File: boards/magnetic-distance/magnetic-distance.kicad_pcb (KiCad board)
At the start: 2 copper layers, 23 x 19.5 mm, 7 parts, among them J1 CONN_02X03, M3 MountingHole_3.2mm_M3, U1 DS9638, U2 AS5304

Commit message: boards/magnetic-distance: reworked sensor placement, updated schematic export
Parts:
- moved AO 5.12 mm to (185.4, 108.0)
- moved U2 1.81 mm to (190.5, 106.5), turned to 0 degrees
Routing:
- net (no net): track 0.00 -> 17.0 mm, vias 23 -> 15
- net /VCC: track 31.3 -> 38.8 mm
- net /GND: track 8.11 -> 10.6 mm
- net /B_c: track 14.9 -> 13.3 mm

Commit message: [docs] export all board layouts
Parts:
- moved J1 127.0 mm to (64.1, 48.3)
- moved AO 127.0 mm to (69.8, 55.2)
- moved C1 127.0 mm to (65.4, 54.9)
- moved U2 127.0 mm to (74.9, 53.8)
- moved M3 127.0 mm to (70.8, 42.1)
- moved M3 127.0 mm to (64.8, 42.1)
- moved U1 127.0 mm to (61.0, 55.9)
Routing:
- net (no net): track 17.0 -> 18.5 mm
- net /GND: track 10.6 -> 9.10 mm

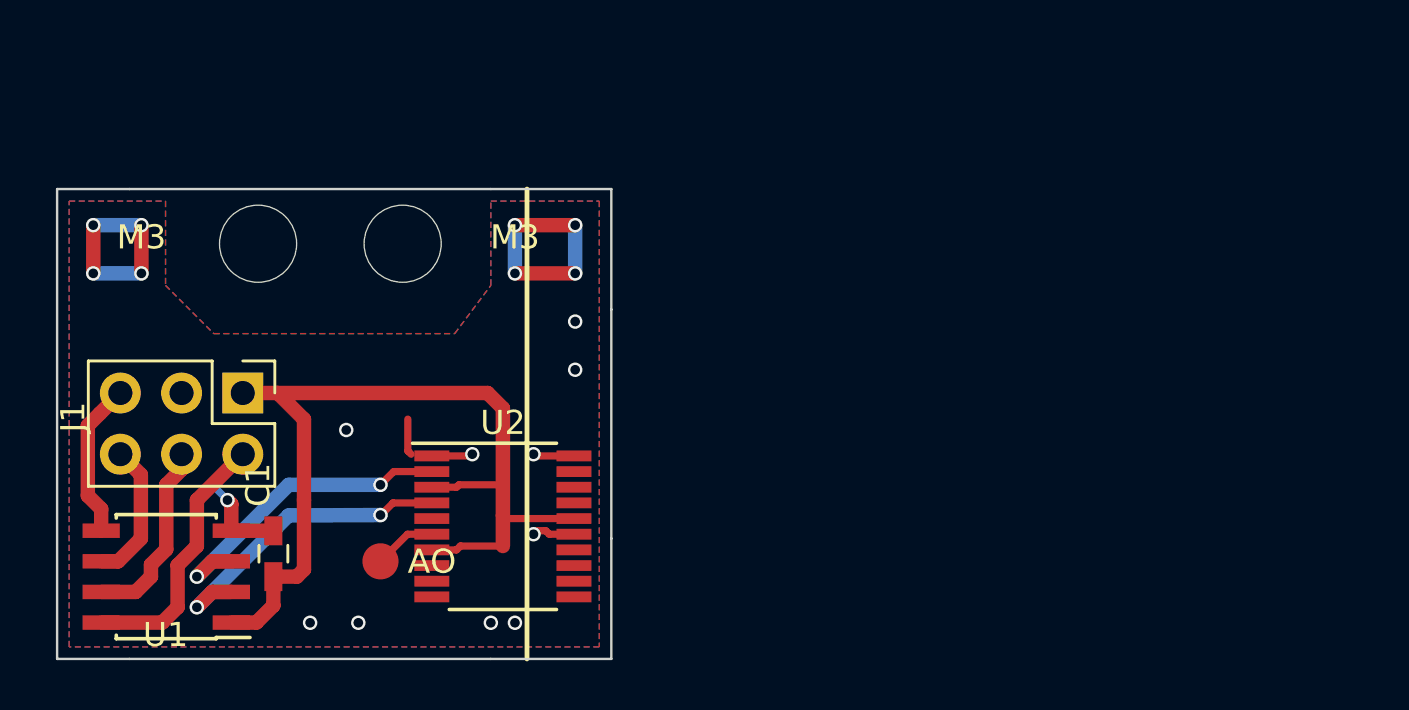
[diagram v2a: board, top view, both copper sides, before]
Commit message: [board][magnetic-distance] remove diff line driver, new board outline
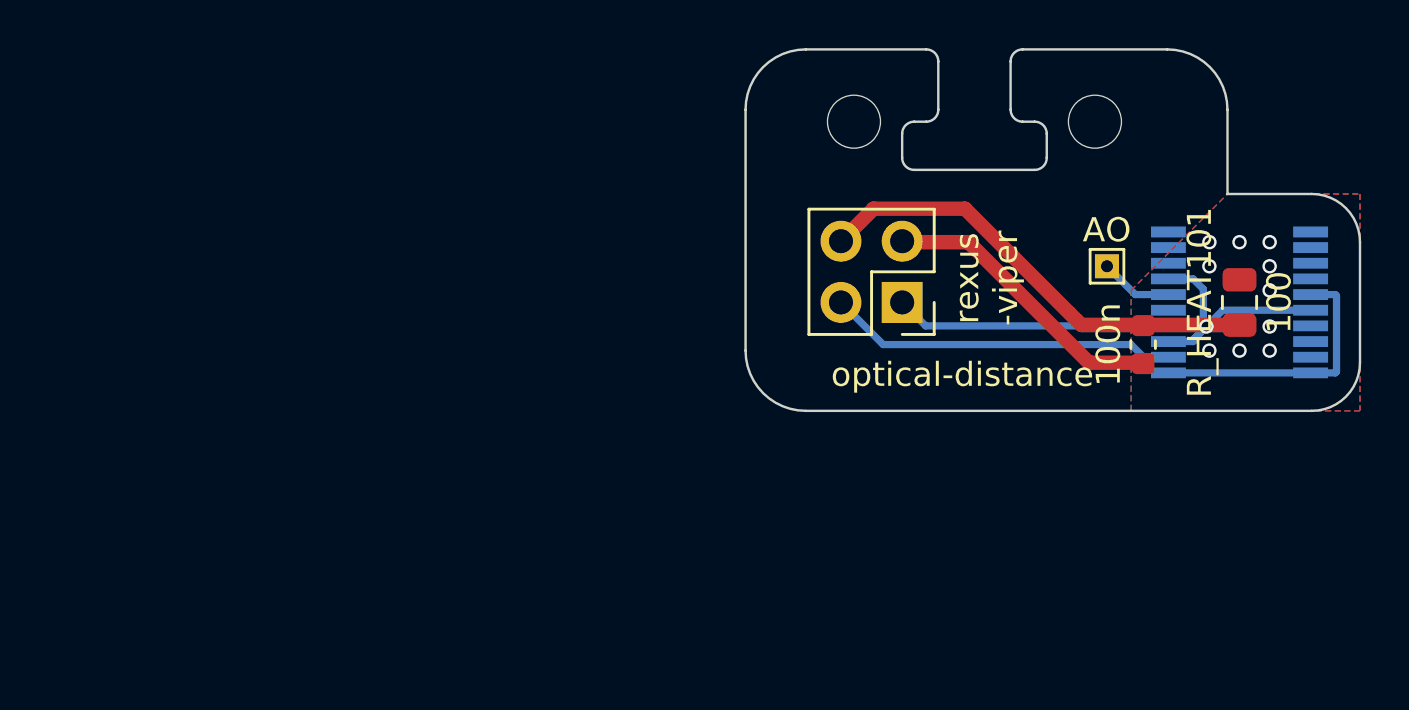
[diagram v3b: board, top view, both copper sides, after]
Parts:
- removed AO: AO, Measurement_Points:Measurement_Point_Round-SMD-Pad_Small
- removed C1: 100nF, Capacitors_SMD:C_0603_HandSoldering
- removed J1: CONN_02X03, Pin_Headers:Pin_Header_Straight_2x03_Pitch2.54mm
- removed M3 (x2): MountingHole_3.2mm_M3, Mounting_Holes:MountingHole_3.2mm_M3
- removed U1: DS9638, Housings_SOIC:SOIC-8_3.9x4.9mm_Pitch1.27mm
- removed U2: AS5304, Housings_SSOP:TSSOP-20_4.4x6.5mm_Pitch0.65mm
- added C101: 100n, Capacitor_SMD:C_0603_1608Metric, F.Cu at (101.5, 46.2)
- added H101: M2, MountingHole:MountingHole_2.2mm_M2, F.Cu at (89.5, 37.0)
- added H102: M2, MountingHole:MountingHole_2.2mm_M2, F.Cu at (99.5, 37.0)
- added J101: Cable, Connector_PinHeader_2.54mm:PinHeader_2x02_P2.54mm_Vertical, F.Cu at (91.5, 44.5)
- added R_HEAT101: 100, Resistor_SMD:R_0805_2012Metric, F.Cu at (105.5, 44.5)
- added TP101: AO, TestPoint:TestPoint_THTPad_1.0x1.0mm_Drill0.5mm, F.Cu at (100.0, 43.0)
- added U101: AS5304, Package_SO:TSSOP-20_4.4x6.5mm_P0.65mm, B.Cu at (105.5, 44.5)
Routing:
- net /VCC: track 38.8 -> 0.00 mm
- net +5V: track 0.00 -> 29.4 mm, vias 0 -> 1
- net GND: track 0.00 -> 23.3 mm, vias 0 -> 10
- net (no net): track 18.5 -> 0.00 mm, vias 15 -> 0
- net /B_c: track 13.3 -> 0.00 mm, vias 2 -> 0
- net /A_c: track 13.2 -> 0.00 mm, vias 2 -> 0
- net /GND: track 9.10 -> 0.00 mm, vias 4 -> 0
- net /A*: track 7.93 -> 0.00 mm
- net /B*: track 6.50 -> 0.00 mm
- net /B: track 5.89 -> 11.5 mm
- net /A: track 10.9 -> 14.5 mm
- added copper zone on B.Cu, net GND
- added copper zone on F.Cu, net GND
- removed copper zone on B.Cu, net /GND
- removed copper zone on F.Cu, net /GND
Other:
- board size 23 x 19.5 mm -> 25.5 x 15 mm
- net class Thin removed
- board text added: "5V"
- board text added: "optical-distance"
- board text added: "rev20"
- board text added: "rexus -viper"
- board text removed: "A*"
- board text removed: "B*"
- board text removed: "VCC"
- board text removed: "rexus-viper magnetic-dis- tance board ©rleh, rchojetzki"

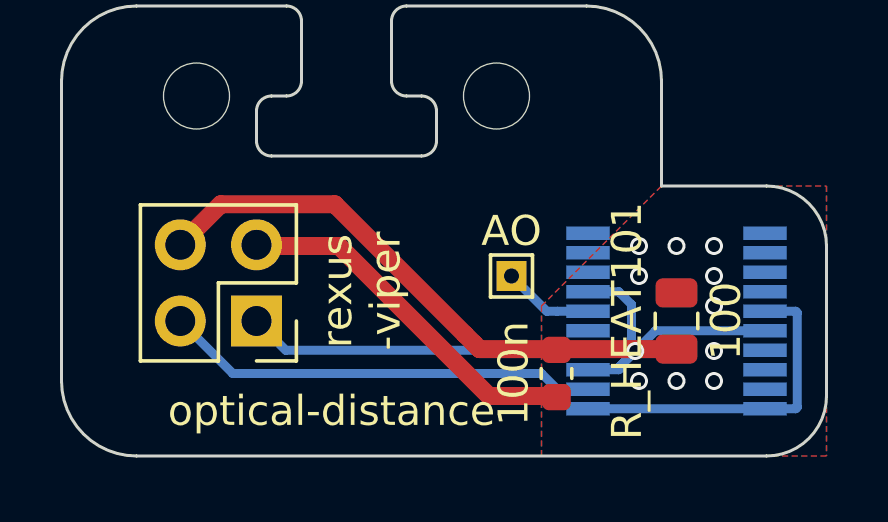
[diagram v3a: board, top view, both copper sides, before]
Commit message: [board][magnetic-distance] sensor placement
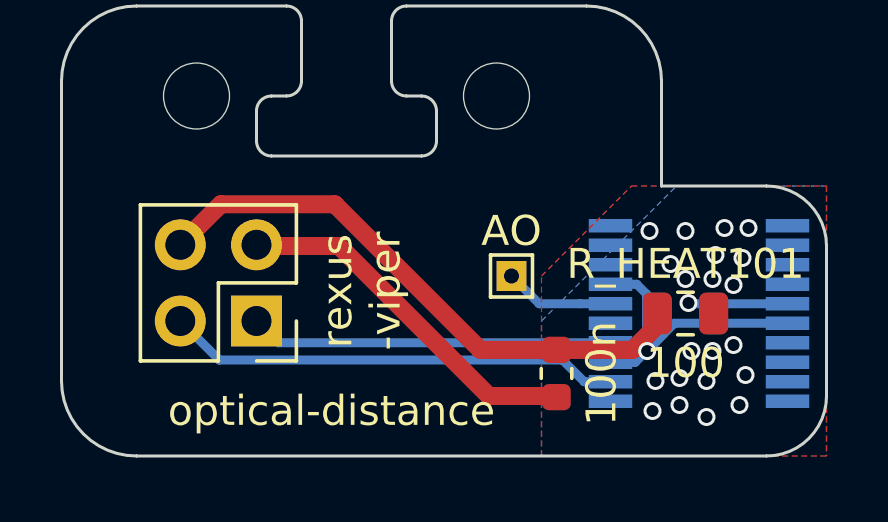
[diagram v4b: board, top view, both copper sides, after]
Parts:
- moved U101 0.79 mm to (106.2, 44.2)
- moved R_HEAT101 0.39 mm to (105.8, 44.2), turned to 0 degrees
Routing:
- net GND: track 23.3 -> 15.6 mm, vias 10 -> 22
- net +5V: track 29.4 -> 31.9 mm
- net /A: track 14.5 -> 15.2 mm
- net /AO: track 3.04 -> 3.68 mm
- net /B: track 11.5 -> 12.1 mm

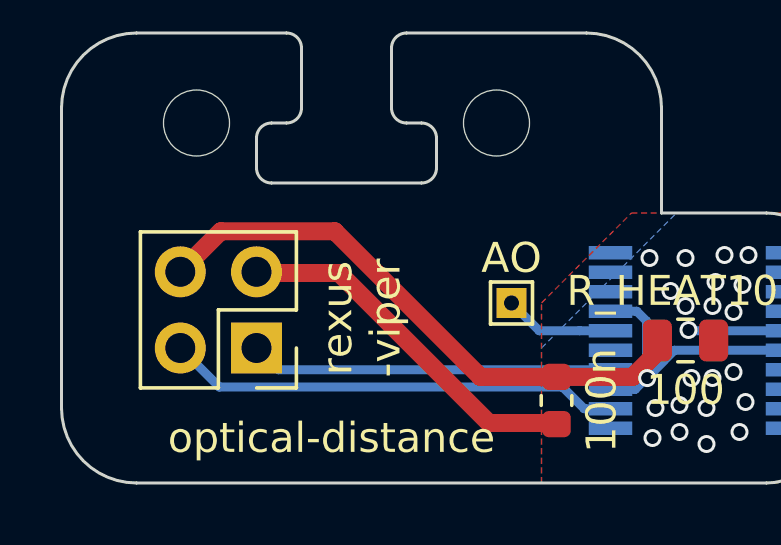
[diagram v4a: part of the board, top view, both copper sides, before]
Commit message: [board][magnetic-distance] add 10µ cap to 5V rail
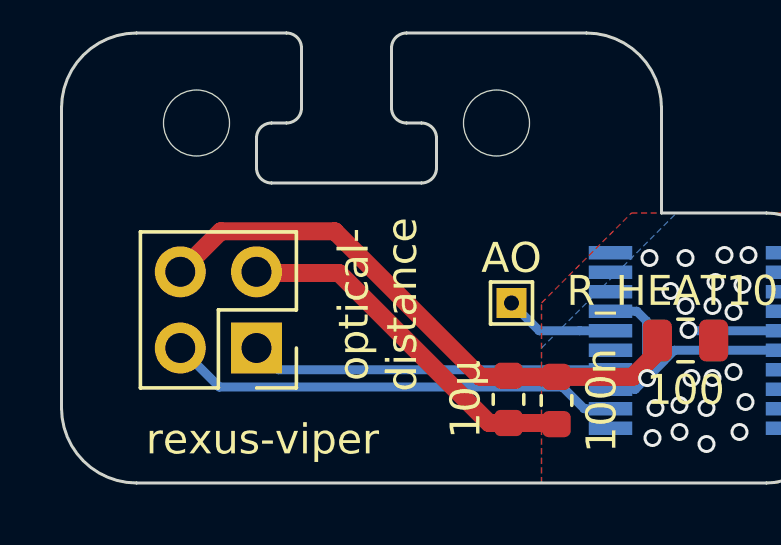
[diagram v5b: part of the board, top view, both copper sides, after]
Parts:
- added C102: 10µ, Capacitor_SMD:C_0603_1608Metric, F.Cu at (99.9, 46.2)
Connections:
- U101 pad 10: Net-(U101-Pad10) -> (no net)
- U101 pad 11: Net-(U101-Pad11) -> (no net)
- U101 pad 12: Net-(U101-Pad12) -> (no net)
- U101 pad 13: Net-(U101-Pad13) -> (no net)
- U101 pad 14: Net-(U101-Pad14) -> (no net)
- U101 pad 17: Net-(U101-Pad17) -> (no net)
- U101 pad 18: Net-(U101-Pad18) -> (no net)
- U101 pad 19: Net-(U101-Pad19) -> (no net)
- U101 pad 5: Net-(U101-Pad5) -> (no net)
- U101 pad 8: Net-(U101-Pad8) -> (no net)
- U101 pad 9: Net-(U101-Pad9) -> (no net)
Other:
- board text added: "optical- distance"
- board text added: "rexus-viper"
- board text removed: "optical-distance"
- board text removed: "rexus -viper"
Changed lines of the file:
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@@
     (tracks 60)
     (zones 0)
-    (modules 7)
-    (nets 17)
+    (modules 8)
+    (nets 6)
   )
   (page User 140.005 119.99)
@@
     (47 F.CrtYd user)
     (48 B.Fab user hide)
-    (49 F.Fab user hide)
+    (49 F.Fab user)
   )
   (setup
-    (last_trace_width 0.3)
+    (last_trace_width 0.6)
     (user_trace_width 0.3)
     (trace_clearance 0.2)
@@
   (net 4 +5V)
   (net 5 GND)
-  (net 6 "Net-(U101-Pad5)")
-  (net 7 "Net-(U101-Pad8)")
-  (net 8 "Net-(U101-Pad9)")
-  (net 9 "Net-(U101-Pad10)")
-  (net 10 "Net-(U101-Pad11)")
-  (net 11 "Net-(U101-Pad12)")
-  (net 12 "Net-(U101-Pad13)")
-  (net 13 "Net-(U101-Pad14)")
-  (net 14 "Net-(U101-Pad17)")
-  (net 15 "Net-(U101-Pad18)")
-  (net 16 "Net-(U101-Pad19)")
   (net_class Default "This is the default net class."
     (clearance 0.2)
@@
     (add_net /B)
     (add_net GND)
-    (add_net "Net-(U101-Pad10)")
-    (add_net "Net-(U101-Pad11)")
-    (add_net "Net-(U101-Pad12)")
-    (add_net "Net-(U101-Pad13)")
-    (add_net "Net-(U101-Pad14)")
-    (add_net "Net-(U101-Pad17)")
-    (add_net "Net-(U101-Pad18)")
-    (add_net "Net-(U101-Pad19)")
-    (add_net "Net-(U101-Pad5)")
-    (add_net "Net-(U101-Pad8)")
-    (add_net "Net-(U101-Pad9)")
   )
   (module Capacitor_SMD:C_0603_1608Metric (layer F.Cu)
@@
       (net 2 /B) (zone_connect 2))
     (pad 5 smd rect (at -2.95 0.325) (size 1.45 0.45) (layers B.Cu B.Paste B.Mask)
-      (net 6 "Net-(U101-Pad5)") (zone_connect 2))
+      (zone_connect 2))
     (pad 6 smd rect (at -2.95 -0.325) (size 1.45 0.45) (layers B.Cu B.Paste B.Mask)
       (net 3 /AO) (zone_connect 2))
@@
       (net 4 +5V) (zone_connect 2))
     (pad 8 smd rect (at -2.95 -1.625) (size 1.45 0.45) (layers B.Cu B.Paste B.Mask)
-      (net 7 "Net-(U101-Pad8)") (zone_connect 2))
+      (zone_connect 2))
     (pad 9 smd rect (at -2.95 -2.275) (size 1.45 0.45) (layers B.Cu B.Paste B.Mask)
-      (net 8 "Net-(U101-Pad9)") (zone_connect 2))
+      (zone_connect 2))
     (pad 10 smd rect (at -2.95 -2.925) (size 1.45 0.45) (layers B.Cu B.Paste B.Mask)
-      (net 9 "Net-(U101-Pad10)") (zone_connect 2))
+      (zone_connect 2))
     (pad 11 smd rect (at 2.95 -2.925) (size 1.45 0.45) (layers B.Cu B.Paste B.Mask)
-      (net 10 "Net-(U101-Pad11)") (zone_connect 2))
+      (zone_connect 2))
     (pad 12 smd rect (at 2.95 -2.275) (size 1.45 0.45) (layers B.Cu B.Paste B.Mask)
-      (net 11 "Net-(U101-Pad12)") (zone_connect 2))
+      (zone_connect 2))
     (pad 13 smd rect (at 2.95 -1.625) (size 1.45 0.45) (layers B.Cu B.Paste B.Mask)
-      (net 12 "Net-(U101-Pad13)") (zone_connect 2))
+      (zone_connect 2))
     (pad 14 smd rect (at 2.95 -0.975) (size 1.45 0.45) (layers B.Cu B.Paste B.Mask)
-      (net 13 "Net-(U101-Pad14)") (zone_connect 2))
+      (zone_connect 2))
     (pad 15 smd rect (at 2.95 -0.325) (size 1.45 0.45) (layers B.Cu B.Paste B.Mask)
       (net 5 GND) (zone_connect 2))
@@
       (net 4 +5V) (zone_connect 2))
     (pad 17 smd rect (at 2.95 0.975) (size 1.45 0.45) (layers B.Cu B.Paste B.Mask)
-      (net 14 "Net-(U101-Pad17)") (zone_connect 2))
+      (zone_connect 2))
     (pad 18 smd rect (at 2.95 1.625) (size 1.45 0.45) (layers B.Cu B.Paste B.Mask)
-      (net 15 "Net-(U101-Pad18)") (zone_connect 2))
+      (zone_connect 2))
     (pad 19 smd rect (at 2.95 2.275) (size 1.45 0.45) (layers B.Cu B.Paste B.Mask)
-      (net 16 "Net-(U101-Pad19)") (zone_connect 2))
+      (zone_connect 2))
     (pad 20 smd rect (at 2.95 2.925) (size 1.45 0.45) (layers B.Cu B.Paste B.Mask)
       (net 5 GND) (zone_connect 2))
@@
     (pad 1 thru_hole rect (at 0 0) (size 1 1) (drill 0.5) (layers *.Cu *.Mask)
       (net 3 /AO))
+  )
+  (module Capacitor_SMD:C_0603_1608Metric (layer F.Cu)
+    (at 99.9 46.2125 270)
+    (descr "Capacitor SMD 0603 (1608 Metric), square (rectangular) end terminal, IPC_7351 nominal, (Body size source: http://www.tortai-tech.com/upload/download/2011102023233369053.pdf), generated with kicad-footprint-generator")
+    (tags capacitor)
+    (attr smd)
+    (fp_text reference C102 (at 0 -1.43 270) (layer F.SilkS) hide
+      (effects (font (size 1 1) (thickness 0.15)))
+    )
+    (fp_text value 10µ (at 0 1.43 270) (layer F.SilkS)
+      (effects (font (size 1 1) (thickness 0.15)))
+    )
+    (fp_line (start -0.8 0.4) (end -0.8 -0.4) (layer F.Fab) (width 0.1))
+    (fp_line (start -0.8 -0.4) (end 0.8 -0.4) (layer F.Fab) (width 0.1))
+    (fp_line (start 0.8 -0.4) (end 0.8 0.4) (layer F.Fab) (width 0.1))
+    (fp_line (start 0.8 0.4) (end -0.8 0.4) (layer F.Fab) (width 0.1))
+    (fp_line (start -0.162779 -0.51) (end 0.162779 -0.51) (layer F.SilkS) (width 0.12))
+    (fp_line (start -0.162779 0.51) (end 0.162779 0.51) (layer F.SilkS) (width 0.12))
+    (fp_line (start -1.48 0.73) (end -1.48 -0.73) (layer F.CrtYd) (width 0.05))
+    (fp_line (start -1.48 -0.73) (end 1.48 -0.73) (layer F.CrtYd) (width 0.05))
+    (fp_line (start 1.48 -0.73) (end 1.48 0.73) (layer F.CrtYd) (width 0.05))
+    (fp_line (start 1.48 0.73) (end -1.48 0.73) (layer F.CrtYd) (width 0.05))
+    (fp_text user %R (at 0 0 270) (layer F.Fab)
+      (effects (font (size 0.4 0.4) (thickness 0.06)))
+    )
+    (pad 1 smd roundrect (at -0.7875 0 270) (size 0.875 0.95) (layers F.Cu F.Paste F.Mask) (roundrect_rratio 0.25)
+      (net 4 +5V))
+    (pad 2 smd roundrect (at 0.7875 0 270) (size 0.875 0.95) (layers F.Cu F.Paste F.Mask) (roundrect_rratio 0.25)
+      (net 5 GND))
+    (model ${KISYS3DMOD}/Capacitor_SMD.3dshapes/C_0603_1608Metric.wrl
+      (at (xyz 0 0 0))
+      (scale (xyz 1 1 1))
+      (rotate (xyz 0 0 0))
+    )
   )
   (gr_line (start 108.5 40) (end 105 40) (layer Cmts.User) (width 0.2))
@@
     (effects (font (size 1.5 1.5) (thickness 0.3)) (justify mirror))
   )
-  (gr_text "rexus\n-viper" (at 95 43.5 90) (layer F.SilkS)
+  (gr_text rexus-viper (at 91.7 47.55) (layer F.SilkS)
     (effects (font (size 1 1) (thickness 0.2)))
   )
-  (gr_text optical-distance (at 94 47.5) (layer F.SilkS)
+  (gr_text "optical-\ndistance" (at 95.55 43.05 90) (layer F.SilkS)
     (effects (font (size 1 1) (thickness 0.2)))
   )
@@
   (segment (start 103.3 46.525) (end 102.425 46.525) (width 0.3) (layer B.Cu) (net 1))
   (segment (start 102.425 46.525) (end 101.7 45.8) (width 0.3) (layer B.Cu) (net 1))
-  (via (at 106 45.5) (size 0.6) (drill 0.4) (layers F.Cu B.Cu) (net 5))
-  (via (at 106.7 45.5) (size 0.6) (drill 0.4) (layers F.Cu B.Cu) (net 5))
-  (via (at 107.4 45.3) (size 0.6) (drill 0.4) (layers F.Cu B.Cu) (net 5))
-  (via (at 107.4 43.3) (size 0.6) (drill 0.4) (layers F.Cu B.Cu) (net 5))
-  (via (at 106.7 43.1) (size 0.6) (drill 0.4) (layers F.Cu B.Cu) (net 5))
-  (via (at 107.8 46.3) (size 0.6) (drill 0.4) (layers F.Cu B.Cu) (net 5))
-  (via (at 106.5 46.5) (size 0.6) (drill 0.4) (layers F.Cu B.Cu) (net 5))
-  (via (at 105.6 46.4) (size 0.6) (drill 0.4) (layers F.Cu B.Cu) (net 5))
-  (via (at 104.8 46.5) (size 0.6) (drill 0.4) (layers F.Cu B.Cu) (net 5))
-  (via (at 107.7 42.4) (size 0.6) (drill 0.4) (layers F.Cu B.Cu) (net 5))
-  (via (at 106.8 42.3) (size 0.6) (drill 0.4) (layers F.Cu B.Cu) (net 5))
-  (via (at 105.3 42.6) (size 0.6) (drill 0.4) (layers F.Cu B.Cu) (net 5))
-  (via (at 104.6 41.5) (size 0.6) (drill 0.4) (layers F.Cu B.Cu) (net 5))
-  (via (at 105.8 41.5) (size 0.6) (drill 0.4) (layers F.Cu B.Cu) (net 5))
-  (via (at 107.1 41.4) (size 0.6) (drill 0.4) (layers F.Cu B.Cu) (net 5))
-  (via (at 107.9 41.4) (size 0.6) (drill 0.4) (layers F.Cu B.Cu) (net 5))
   (segment (start 101.775 45.225) (end 103.3 45.225) (width 0.3) (layer B.Cu) (net 2))
   (segment (start 91.5 44.5) (end 92.225 45.225) (width 0.3) (layer B.Cu) (net 2))
@@
   (segment (start 101.5 45.4625) (end 104.0375 45.4625) (width 0.6) (layer F.Cu) (net 4))
   (segment (start 104.0375 45.4625) (end 104.8625 44.6375) (width 0.6) (layer F.Cu) (net 4))
+  (via (at 106 45.5) (size 0.6) (drill 0.4) (layers F.Cu B.Cu) (net 5))
+  (via (at 106.7 45.5) (size 0.6) (drill 0.4) (layers F.Cu B.Cu) (net 5))
+  (via (at 107.4 45.3) (size 0.6) (drill 0.4) (layers F.Cu B.Cu) (net 5))
+  (via (at 107.4 43.3) (size 0.6) (drill 0.4) (layers F.Cu B.Cu) (net 5))
+  (via (at 106.7 43.1) (size 0.6) (drill 0.4) (layers F.Cu B.Cu) (net 5))
+  (via (at 107.8 46.3) (size 0.6) (drill 0.4) (layers F.Cu B.Cu) (net 5))
+  (via (at 106.5 46.5) (size 0.6) (drill 0.4) (layers F.Cu B.Cu) (net 5))
+  (via (at 105.6 46.4) (size 0.6) (drill 0.4) (layers F.Cu B.Cu) (net 5))
+  (via (at 104.8 46.5) (size 0.6) (drill 0.4) (layers F.Cu B.Cu) (net 5))
+  (via (at 107.7 42.4) (size 0.6) (drill 0.4) (layers F.Cu B.Cu) (net 5))
+  (via (at 106.8 42.3) (size 0.6) (drill 0.4) (layers F.Cu B.Cu) (net 5))
+  (via (at 105.3 42.6) (size 0.6) (drill 0.4) (layers F.Cu B.Cu) (net 5))
+  (via (at 104.6 41.5) (size 0.6) (drill 0.4) (layers F.Cu B.Cu) (net 5))
+  (via (at 105.8 41.5) (size 0.6) (drill 0.4) (layers F.Cu B.Cu) (net 5))
+  (via (at 107.1 41.4) (size 0.6) (drill 0.4) (layers F.Cu B.Cu) (net 5))
+  (via (at 107.9 41.4) (size 0.6) (drill 0.4) (layers F.Cu B.Cu) (net 5))
   (segment (start 94.25 42) (end 91.54 42) (width 0.6) (layer F.Cu) (net 5))
   (segment (start 99.25 47) (end 94.25 42) (width 0.6) (layer F.Cu) (net 5))
